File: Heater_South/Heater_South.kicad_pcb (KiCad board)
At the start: 2 copper layers, 52.1 x 57.1 mm, 8 parts, among them J1 SHB1, J2 SHB2, J3 Heater South

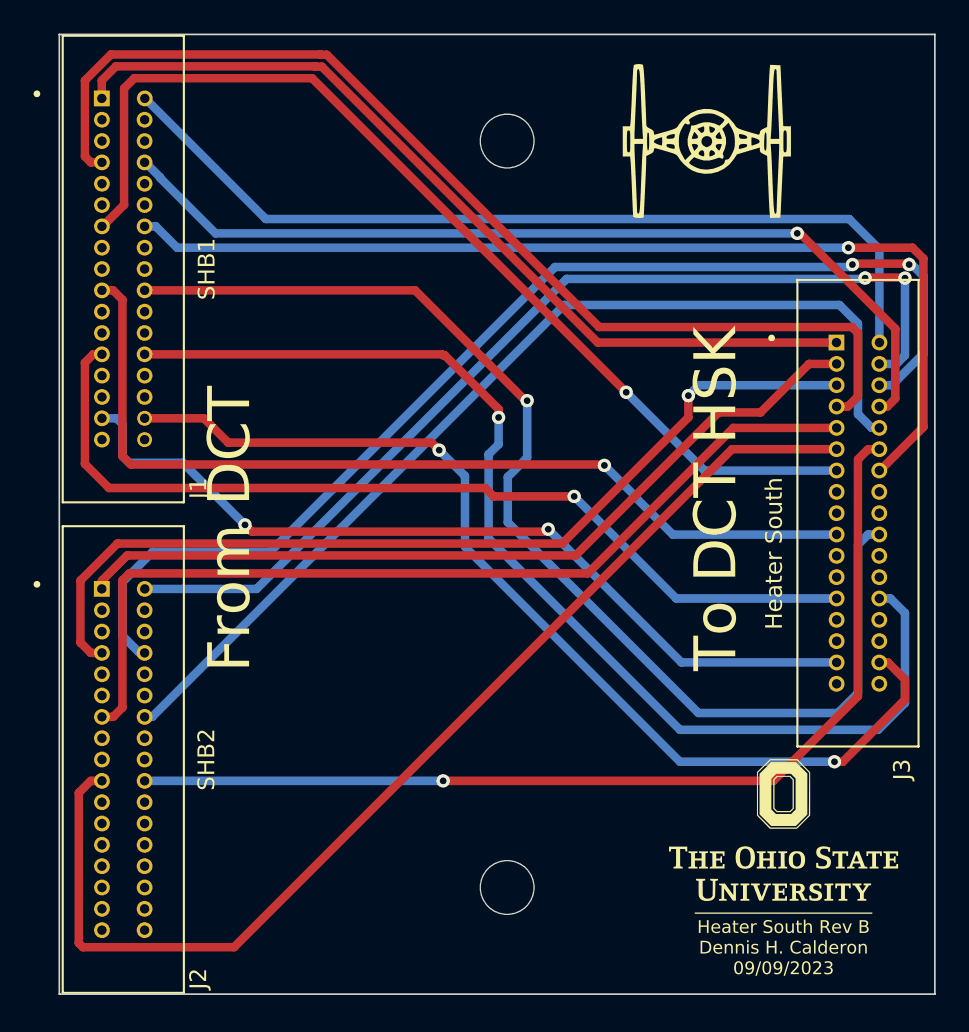
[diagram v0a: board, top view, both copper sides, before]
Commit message: Updated Heater South with correct mapping referencing DCT_Heater_Driver schematic. Updated silscreen on all boards. Generated fabrication files.
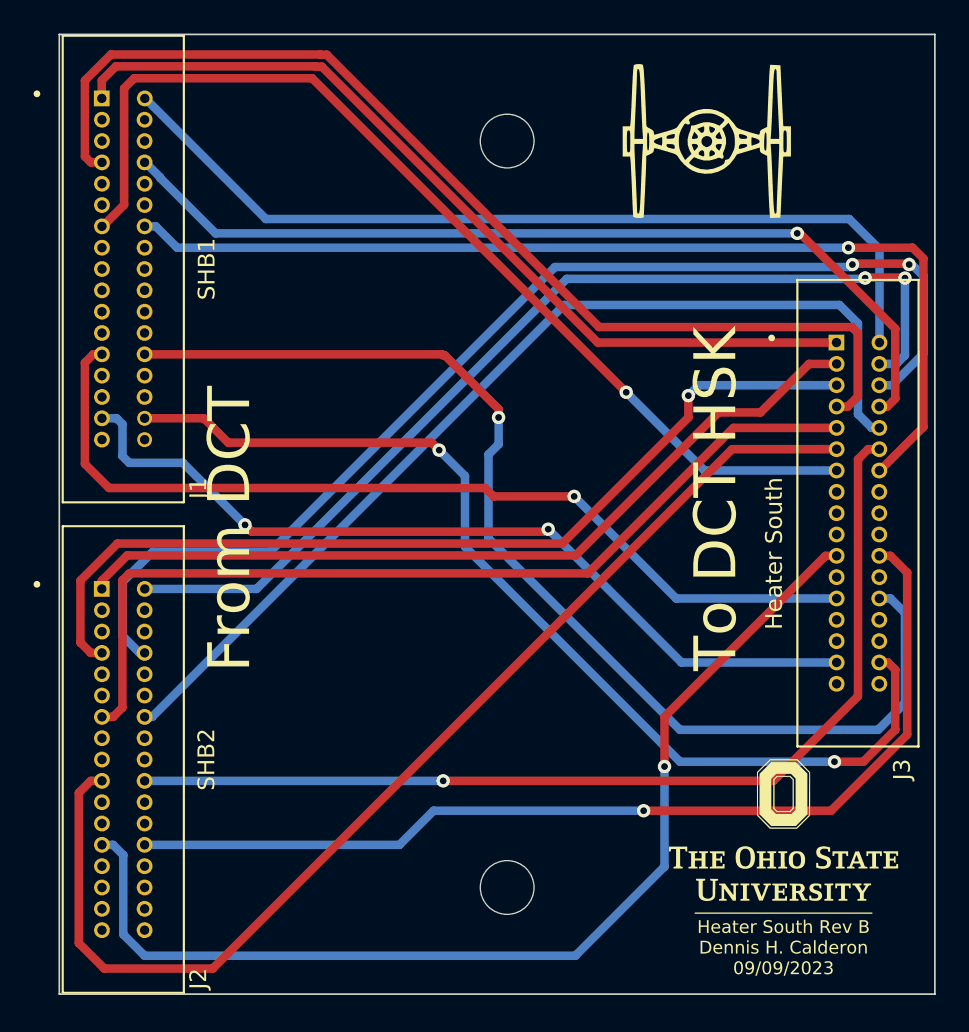
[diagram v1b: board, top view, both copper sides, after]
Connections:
- J1 pad 19: /HB1_19 -> unconnected-(J1-Pin_19-Pad19)
- J1 pad 20: /HB1_20 -> unconnected-(J1-Pin_20-Pad20)
- J2 pad 25: unconnected-(J2-Pin_25-Pad25) -> /HB2_25
- J2 pad 26: unconnected-(J2-Pin_26-Pad26) -> /HB2_26
- J3 pad 19: /HB1_19 -> unconnected-(J3-Pin_19-Pad19)
- J3 pad 20: /HB1_20 -> unconnected-(J3-Pin_20-Pad20)
- J3 pad 21: unconnected-(J3-Pin_21-Pad21) -> /HB2_25
- J3 pad 22: unconnected-(J3-Pin_22-Pad22) -> /HB2_26
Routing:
- net /HB1_20: track 69.6 -> 0.00 mm, vias 1 -> 0
- net /HB2_25: track 0.00 -> 64.3 mm, vias 0 -> 1
- net /HB2_26: track 0.00 -> 59.9 mm, vias 0 -> 1
- net /HB1_19: track 55.3 -> 0.00 mm, vias 1 -> 0
- net /HB2_19: track 68.1 -> 69.2 mm

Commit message: I was working towards fabrication. Chaged the KiCAD violation issues for each PCB to run all tests and make some important silkscreen font bigger. I also edited a few traces and even removed a few vias to make the trace clearance to the edge of the PCBs larger. Need to add the correct centers for the 34-pin connectors on each PCB, rerun traces, and then we should be good.
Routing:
- net /HB1_7: track 64.5 -> 59.8 mm, vias 0 -> 1
- net /HB1_8: track 54.1 -> 56.6 mm
- net /HB1_32: track 61.1 -> 59.6 mm
- net /HB2_2: track 59.6 -> 58.4 mm, vias 2 -> 0
- net /HB2_25: track 64.3 -> 65.4 mm
- net /HB1_26: track 67.8 -> 66.8 mm
- net /HB2_7: track 55.8 -> 55.1 mm
- net /HB2_8: track 68.9 -> 68.3 mm, vias 2 -> 0
- net /HB1_2: track 53.0 -> 52.8 mm, vias 0 -> 1
